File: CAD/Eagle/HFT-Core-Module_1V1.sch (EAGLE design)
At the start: 399 parts, among them Q0521 ABS07-32.768KHZ, Q0811 ABM03B-32.000MHZ, Q0911 ABM3B-16MHZ-10-R50-1-U, T1201 MMBT2222, T1202 MMBT2222, T1203 MMBT2222, U0111 STM32L4Z_144PIN_SMPS, U0431 PAM2305AAB120, U0601 LM4120IM5-3.0, U0611 MAX5217, U0631 CFPT-141-20MHZ, U0641 OPA354, U0701 Si5338, U0801 SX1276, U0901 AX5243, U0911 PE4259, U0921 PE4259, U0991 PE4259, U1101 MCP3911A0-E-SS, U1111 MAX5136AGTG+, U1121 OPA354, U1131 OPA354, U1141 OPA354, U1201 NHD-C0220BIZ_2X20CHARS, U1301 MPU-9250, U1311 MS5607-02BA03, U1321 SHT31-DIS, U1402 SPV1040T, U1501 TS5A23166, U1601 SC189ZSKTRT, U1701 TS5A23166, U1801 TS5A23166, U1901 TS5A23166, X1261 TTE_EN11-HSM, X1401 WIRE-TO-BOARD_5MM08_1X02, X2001 MOLEX 105017-0001, X2101 SMA_SMT_AMPHENOL-901-143, SAM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, X2111 SMA_SMT_AMPHENOL-901-143, SAM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, X2201 CUI SJ1-3535NS, X2211 CUI SJ1-3535NS, X2311 2X20/90_1MM27_HARWIN_M50-3202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, X2312 2X20/90_1MM27_HARWIN_M50-3202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, X2321 2X20/90_1MM27_HARWIN_M50-3202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, X2322 2X20/90_1MM27_HARWIN_M50-3202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, X2331 2X20/90_1MM27_HARWIN_M50-3202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, X2332 2X20/90_1MM27_HARWIN_M50-3202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

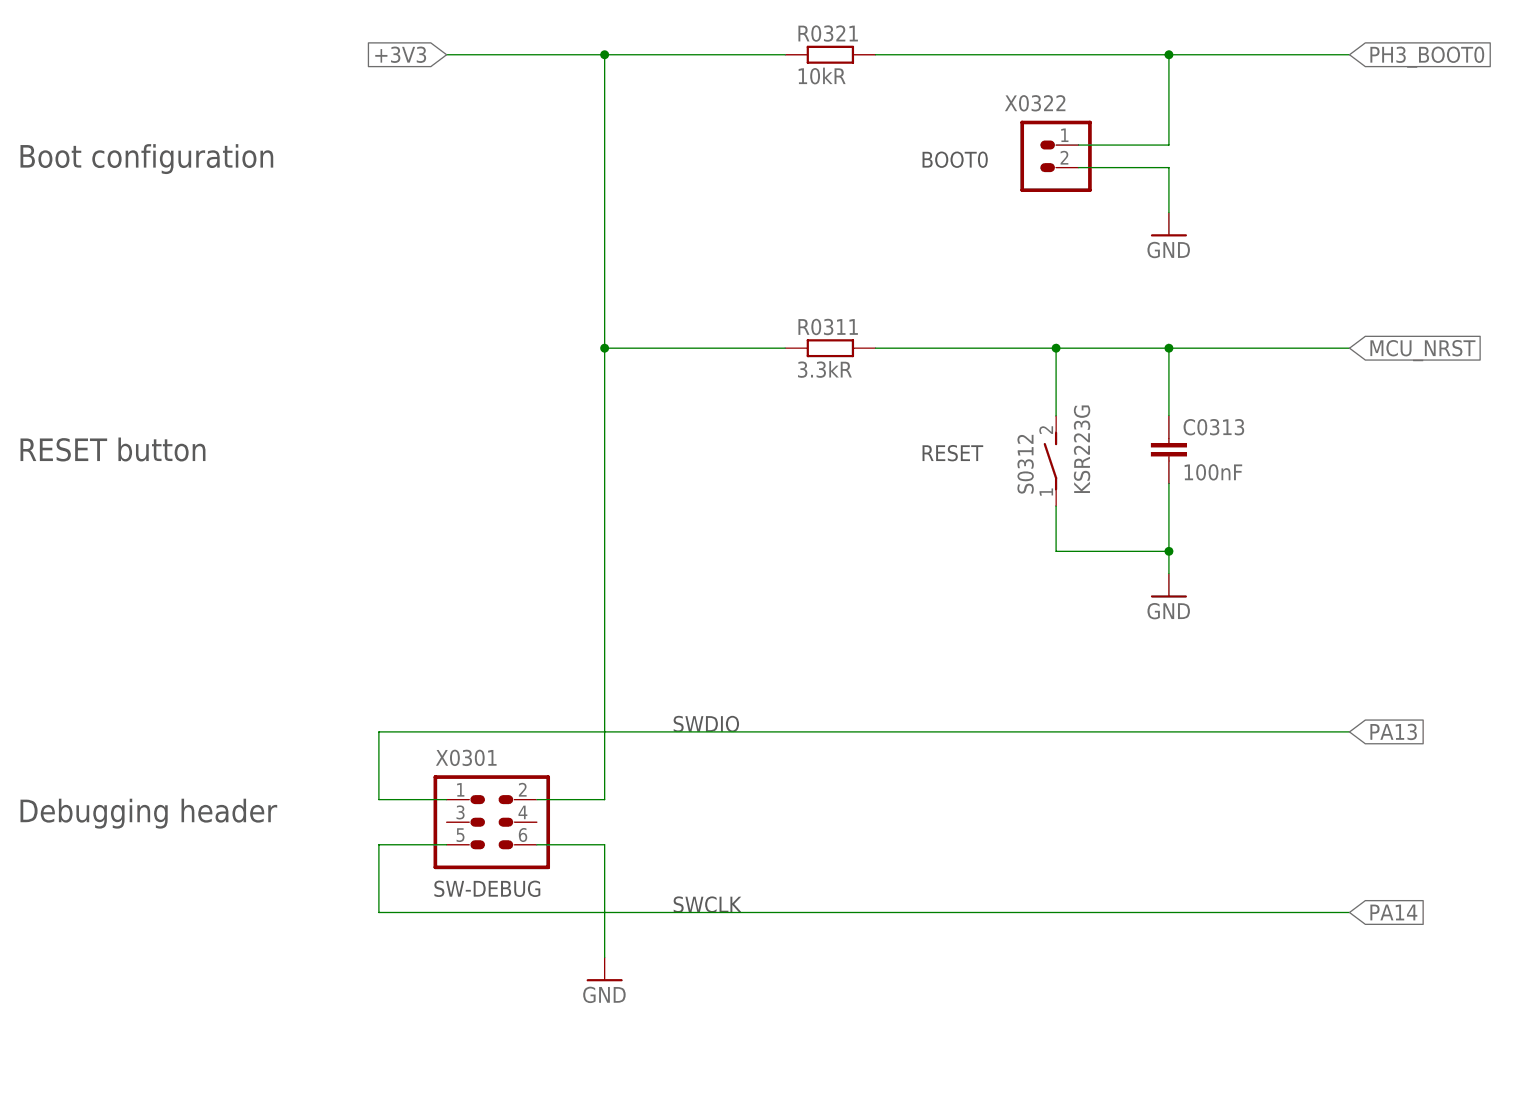
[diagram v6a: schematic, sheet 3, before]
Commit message: HW_1V1 - CAD/Eagle - programmer socket changed, Reset button is of type NO and not NC
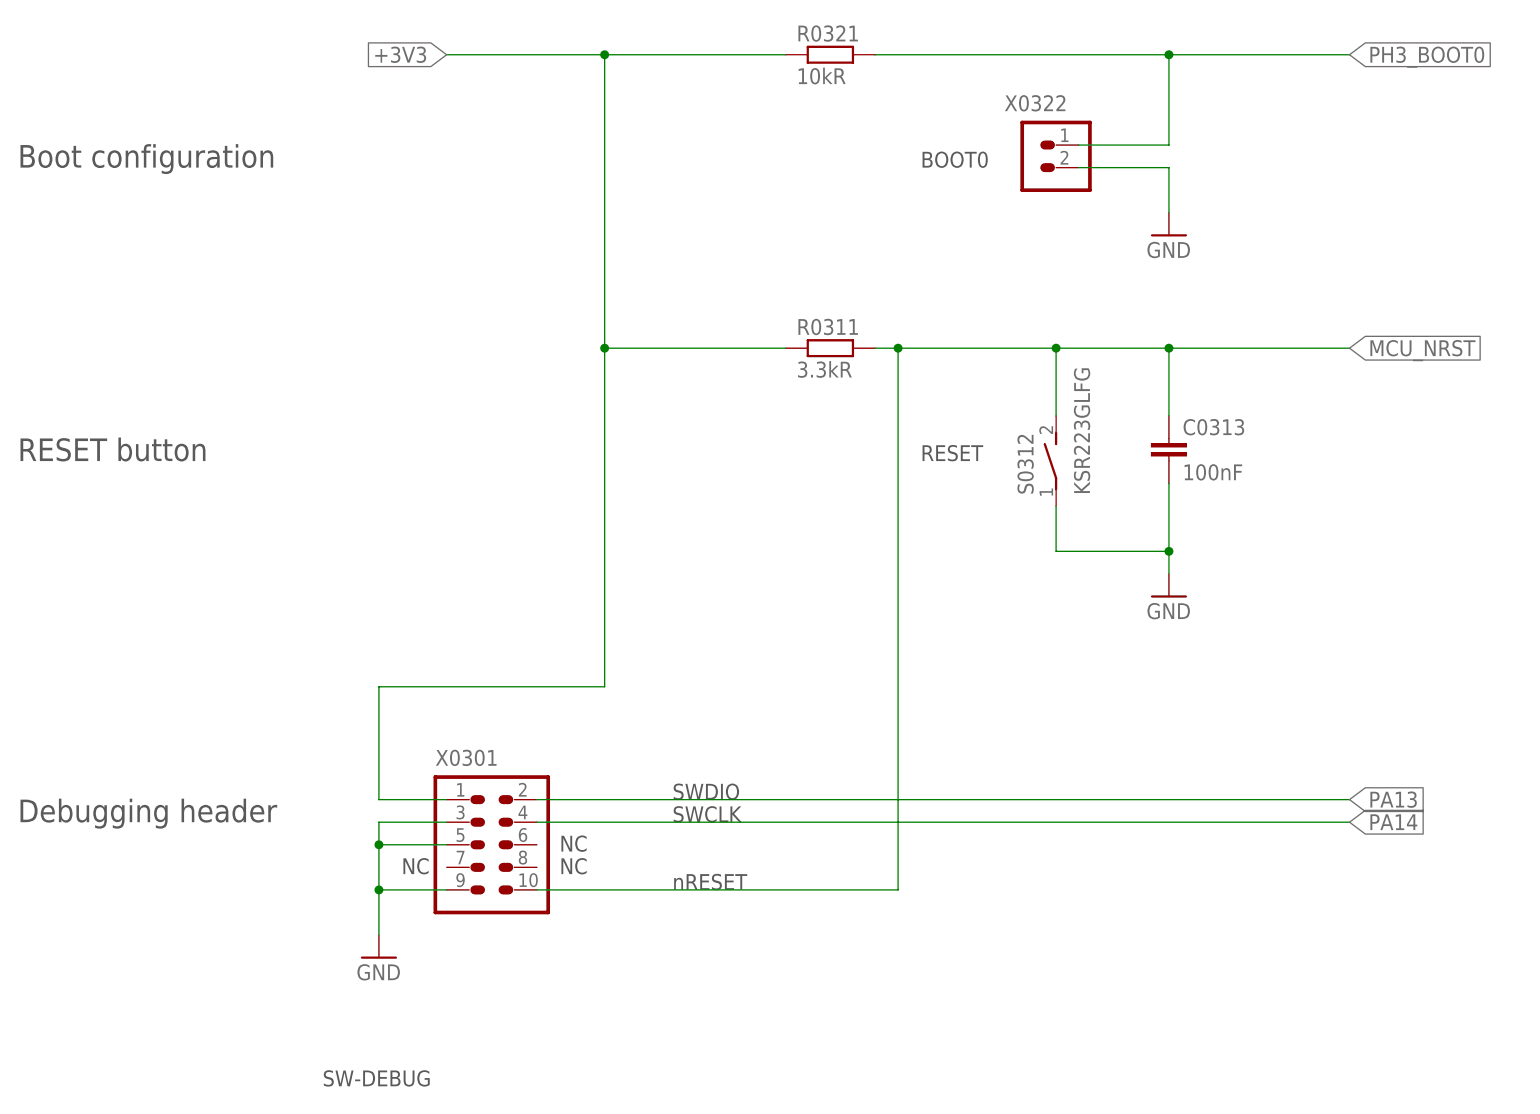
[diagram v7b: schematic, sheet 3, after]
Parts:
- R1201: value 1.8kR -> 2.0kR
- R1202: value 5.2kR -> 1.5kR
- R1203: value 68R -> 27R
- S0312: value KSR223G -> KSR223GLFG
- X0301: device df4iah_connector:HEADER-2X3 -> df4iah_connector:HEADER-2X5_1MM27CORTEX_10PIN_JTAG-SWD
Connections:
- net +3V3: now also X0301.1; no longer X0301.2
- net GND: now also X0301.3, X0301.5, X0301.9; no longer X0301.6
- net MCU_NRST: now also X0301.10
- net PA13: now also X0301.2; no longer X0301.1
- net PA14: now also X0301.4; no longer X0301.5
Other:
- note added: "Test-Value"
- note added: "nRESET"
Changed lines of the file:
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@@
 <part name="C1605" library="rcl" deviceset="C-EU" device="C0603" value="100nF"/>
 <part name="C1606" library="rcl" deviceset="C-EU" device="C0805" value="47uF"/>
-<part name="X0301" library="df4iah_connector" deviceset="HEADER-2X3" device=""/>
+<part name="X0301" library="df4iah_connector" deviceset="HEADER-2X5_1MM27" device="CORTEX_10PIN_JTAG-SWD"/>
 <part name="GND0301" library="df4iah_supply" deviceset="GND" device=""/>
 <part name="X0322" library="df4iah_connector" deviceset="HEADER-1X2" device=""/>
@@
 <part name="X2322" library="df4iah_connector" deviceset="2X20/90_1MM27_HARWIN_M50-3202045" device=""/>
 <part name="X2332" library="df4iah_connector" deviceset="2X20/90_1MM27_HARWIN_M50-3202045" device=""/>
-<part name="S0312" library="df4iah_switch" deviceset="KSR223G_SMD_1POL" device="" value="KSR223G"/>
+<part name="S0312" library="df4iah_switch" deviceset="KSR223G_SMD_1POL" device="" value="KSR223GLFG"/>
 <part name="U1601" library="df4iah_powersupply" deviceset="PAM2305" device="" value="SC189ZSKTRT"/>
 <part name="U1402" library="df4iah_powersupply" deviceset="SPV1040" device="" value="SPV1040T"/>
@@
 <part name="R1207" library="rcl" deviceset="R-EU_" device="R0603" value="2.2kR"/>
 <part name="R1206" library="rcl" deviceset="R-EU_" device="R0805" value="10R"/>
-<part name="R1203" library="rcl" deviceset="R-EU_" device="R0805" value="68R"/>
+<part name="R1203" library="rcl" deviceset="R-EU_" device="R0805" value="27R"/>
 <part name="R1205" library="rcl" deviceset="R-EU_" device="R0603" value="1.8kR"/>
-<part name="R1202" library="rcl" deviceset="R-EU_" device="R0603" value="5.2kR"/>
+<part name="R1202" library="rcl" deviceset="R-EU_" device="R0603" value="1.5kR"/>
 <part name="R1204" library="rcl" deviceset="R-EU_" device="R0603" value="2.2kR"/>
-<part name="R1201" library="rcl" deviceset="R-EU_" device="R0603" value="1.8kR"/>
+<part name="R1201" library="rcl" deviceset="R-EU_" device="R0603" value="2.0kR"/>
 <part name="FRAME_13" library="df4iah_frame" deviceset="A4L-LOC" device="" value="Holes"/>
 <part name="U1301" library="df4iah_sensors" deviceset="MPU-9250" device="" value="MPU-9250"/>
@@
 <description>MCU Debug</description>
 <plain>
-<text x="99.06" y="73.66" size="1.778" layer="97">SWDIO</text>
-<text x="99.06" y="53.34" size="1.778" layer="97">SWCLK</text>
+<text x="99.06" y="66.04" size="1.778" layer="97">SWDIO</text>
+<text x="99.06" y="63.5" size="1.778" layer="97">SWCLK</text>
 <text x="127" y="104.14" size="1.778" layer="97">RESET</text>
 <text x="127" y="137.16" size="1.778" layer="97">BOOT0</text>
-<text x="72.136" y="55.118" size="1.778" layer="97">SW-DEBUG</text>
+<text x="59.69" y="33.782" size="1.778" layer="97">SW-DEBUG</text>
 <text x="25.4" y="63.5" size="2.54" layer="97" ratio="15">Debugging header</text>
 <text x="25.4" y="137.16" size="2.54" layer="97" ratio="15">Boot configuration</text>
 <text x="25.4" y="104.14" size="2.54" layer="97" ratio="15">RESET button</text>
+<text x="68.58" y="57.658" size="1.778" layer="97">NC</text>
+<text x="86.36" y="60.198" size="1.778" layer="97">NC</text>
+<text x="86.36" y="57.658" size="1.778" layer="97">NC</text>
+<text x="99.06" y="55.88" size="1.778" layer="97">nRESET</text>
 </plain>
 <instances>
 <instance part="FRAME_03" gate="G$1" x="0" y="0"/>
-<instance part="X0301" gate="G$1" x="78.74" y="63.5"/>
-<instance part="GND0301" gate="1" x="91.44" y="45.72"/>
+<instance part="X0301" gate="G$1" x="78.74" y="60.96"/>
+<instance part="GND0301" gate="1" x="66.04" y="48.26"/>
 <instance part="X0322" gate="A" x="142.24" y="139.7" rot="MR0"/>
 <instance part="GND0321" gate="1" x="154.94" y="129.54"/>
@@
 <pinref part="C0313" gate="G$1" pin="1"/>
 <wire x1="154.94" y1="116.84" x2="142.24" y2="116.84" width="0.1524" layer="91"/>
-<wire x1="142.24" y1="116.84" x2="121.92" y2="116.84" width="0.1524" layer="91"/>
+<wire x1="142.24" y1="116.84" x2="124.46" y2="116.84" width="0.1524" layer="91"/>
+<wire x1="124.46" y1="116.84" x2="121.92" y2="116.84" width="0.1524" layer="91"/>
 <wire x1="154.94" y1="116.84" x2="154.94" y2="109.22" width="0.1524" layer="91"/>
 <junction x="154.94" y="116.84"/>
@@
 <pinref part="S0312" gate="G$1" pin="S"/>
 <wire x1="142.24" y1="116.84" x2="142.24" y2="109.22" width="0.1524" layer="91"/>
+<wire x1="124.46" y1="116.84" x2="124.46" y2="55.88" width="0.1524" layer="91"/>
+<wire x1="124.46" y1="55.88" x2="83.82" y2="55.88" width="0.1524" layer="91"/>
+<junction x="124.46" y="116.84"/>
+<pinref part="X0301" gate="G$1" pin="10"/>
 </segment>
 </net>
@@
 <net name="PA13" class="0">
 <segment>
-<label x="175.26" y="73.66" size="1.778" layer="95" xref="yes"/>
-<wire x1="175.26" y1="73.66" x2="66.04" y2="73.66" width="0.1524" layer="91"/>
-<wire x1="66.04" y1="73.66" x2="66.04" y2="66.04" width="0.1524" layer="91"/>
-<pinref part="X0301" gate="G$1" pin="1"/>
-<wire x1="66.04" y1="66.04" x2="73.66" y2="66.04" width="0.1524" layer="91"/>
+<label x="175.26" y="66.04" size="1.778" layer="95" xref="yes"/>
+<wire x1="175.26" y1="66.04" x2="83.82" y2="66.04" width="0.1524" layer="91"/>
+<pinref part="X0301" gate="G$1" pin="2"/>
 </segment>
 </net>
 <net name="PA14" class="0">
 <segment>
-<wire x1="66.04" y1="53.34" x2="175.26" y2="53.34" width="0.1524" layer="91"/>
-<label x="175.26" y="53.34" size="1.778" layer="95" xref="yes"/>
-<wire x1="66.04" y1="53.34" x2="66.04" y2="60.96" width="0.1524" layer="91"/>
-<pinref part="X0301" gate="G$1" pin="5"/>
-<wire x1="66.04" y1="60.96" x2="73.66" y2="60.96" width="0.1524" layer="91"/>
+<wire x1="83.82" y1="63.5" x2="175.26" y2="63.5" width="0.1524" layer="91"/>
+<label x="175.26" y="63.5" size="1.778" layer="95" xref="yes"/>
+<pinref part="X0301" gate="G$1" pin="4"/>
 </segment>
 </net>
 <net name="GND" class="0">
 <segment>
-<pinref part="X0301" gate="G$1" pin="6"/>
-<wire x1="83.82" y1="60.96" x2="91.44" y2="60.96" width="0.1524" layer="91"/>
-<wire x1="91.44" y1="60.96" x2="91.44" y2="48.26" width="0.1524" layer="91"/>
+<wire x1="66.04" y1="63.5" x2="66.04" y2="60.96" width="0.1524" layer="91"/>
 <pinref part="GND0301" gate="1" pin="GND"/>
+<pinref part="X0301" gate="G$1" pin="3"/>
+<wire x1="66.04" y1="60.96" x2="66.04" y2="55.88" width="0.1524" layer="91"/>
+<wire x1="66.04" y1="55.88" x2="66.04" y2="50.8" width="0.1524" layer="91"/>
+<wire x1="66.04" y1="63.5" x2="73.66" y2="63.5" width="0.1524" layer="91"/>
+<pinref part="X0301" gate="G$1" pin="5"/>
+<wire x1="66.04" y1="60.96" x2="73.66" y2="60.96" width="0.1524" layer="91"/>
+<junction x="66.04" y="60.96"/>
+<pinref part="X0301" gate="G$1" pin="9"/>
+<wire x1="66.04" y1="55.88" x2="73.66" y2="55.88" width="0.1524" layer="91"/>
+<junction x="66.04" y="55.88"/>
 </segment>
 <segment>
@@
 <wire x1="91.44" y1="149.86" x2="111.76" y2="149.86" width="0.1524" layer="91"/>
 <wire x1="91.44" y1="149.86" x2="91.44" y2="116.84" width="0.1524" layer="91"/>
-<pinref part="X0301" gate="G$1" pin="2"/>
-<wire x1="91.44" y1="116.84" x2="91.44" y2="66.04" width="0.1524" layer="91"/>
-<wire x1="83.82" y1="66.04" x2="91.44" y2="66.04" width="0.1524" layer="91"/>
+<wire x1="91.44" y1="116.84" x2="91.44" y2="78.74" width="0.1524" layer="91"/>
 <pinref part="R0311" gate="G$1" pin="1"/>
 <wire x1="91.44" y1="116.84" x2="111.76" y2="116.84" width="0.1524" layer="91"/>
 <junction x="91.44" y="116.84"/>
 <junction x="91.44" y="149.86"/>
+<wire x1="91.44" y1="78.74" x2="66.04" y2="78.74" width="0.1524" layer="91"/>
+<wire x1="66.04" y1="78.74" x2="66.04" y2="66.04" width="0.1524" layer="91"/>
+<pinref part="X0301" gate="G$1" pin="1"/>
+<wire x1="66.04" y1="66.04" x2="73.66" y2="66.04" width="0.1524" layer="91"/>
 </segment>
 </net>
@@
 <text x="195.58" y="53.34" size="1.778" layer="97">MCU_IN_RE_Q</text>
 <text x="195.58" y="35.56" size="1.778" layer="97">MCU_IN_RE_PB</text>
+<text x="12.7" y="88.9" size="1.778" layer="97" rot="R90">Test-Value</text>
+<text x="12.7" y="121.92" size="1.778" layer="97" rot="R90">Test-Value</text>
+<text x="30.48" y="88.9" size="1.778" layer="97" rot="R90">Test-Value</text>
 </plain>
 <instances>
